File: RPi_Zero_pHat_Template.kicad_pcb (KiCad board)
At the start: 2 copper layers, 65 x 30.5 mm, 6 parts, among them J1 RPi_GPIO, J2 RPi_GPIO

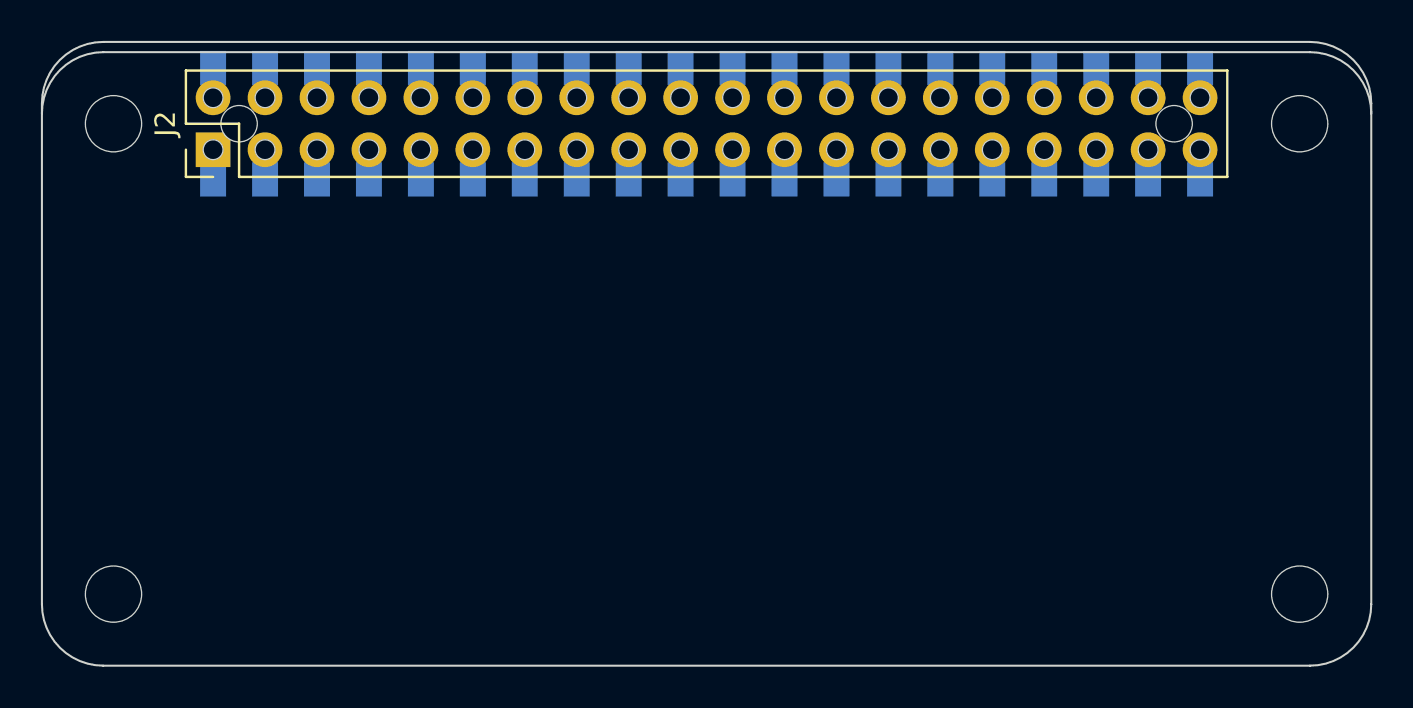
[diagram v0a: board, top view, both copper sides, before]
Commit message: Update to KiCad 8.0.3
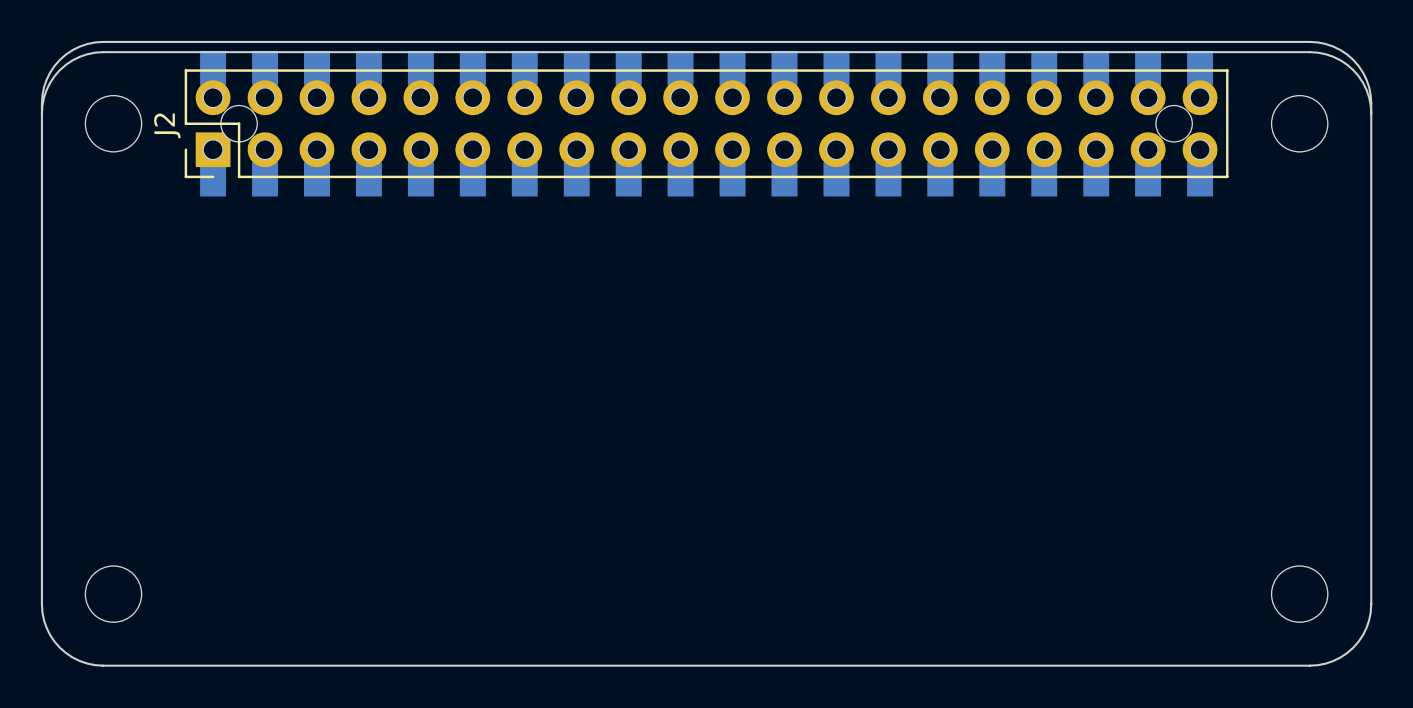
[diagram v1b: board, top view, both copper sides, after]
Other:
- net class Default removed
